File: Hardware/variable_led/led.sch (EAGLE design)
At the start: 12 parts

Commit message: Updated schematic labels and PCB layout based on feedback
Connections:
- net N$1 renamed 5V
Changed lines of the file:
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@@
 <setting verticaltext="up"/>
 </settings>
-<grid distance="0.1" unitdist="inch" unit="inch" style="lines" multiple="1" display="yes" altdistance="0.01" altunitdist="inch" altunit="inch"/>
+<grid distance="0.1" unitdist="inch" unit="inch" style="lines" multiple="1" display="no" altdistance="0.01" altunitdist="inch" altunit="inch"/>
 <layers>
 <layer number="1" name="Top" color="4" fill="1" visible="no" active="no"/>
@@
 </segment>
 </net>
-<net name="N$1" class="0">
+<net name="N$2" class="0">
+<segment>
+<wire x1="68.58" y1="50.8" x2="60.96" y2="50.8" width="0.1524" layer="91"/>
+<wire x1="60.96" y1="50.8" x2="60.96" y2="96.52" width="0.1524" layer="91"/>
+<wire x1="60.96" y1="96.52" x2="111.76" y2="96.52" width="0.1524" layer="91"/>
+<pinref part="R2" gate="G$1" pin="2"/>
+<wire x1="111.76" y1="96.52" x2="111.76" y2="78.74" width="0.1524" layer="91"/>
+<pinref part="JP1" gate="A" pin="13"/>
+</segment>
+</net>
+<net name="N$3" class="0">
+<segment>
+<pinref part="R2" gate="G$1" pin="1"/>
+<pinref part="LED1" gate="G$1" pin="A"/>
+<wire x1="111.76" y1="68.58" x2="111.76" y2="60.96" width="0.1524" layer="91"/>
+</segment>
+</net>
+<net name="N$4" class="0">
+<segment>
+<pinref part="SW1" gate="G$1" pin="P$1"/>
+<pinref part="R1" gate="G$1" pin="2"/>
+<wire x1="12.7" y1="22.86" x2="12.7" y2="20.32" width="0.1524" layer="91"/>
+<wire x1="12.7" y1="20.32" x2="58.42" y2="20.32" width="0.1524" layer="91"/>
+<wire x1="58.42" y1="20.32" x2="58.42" y2="81.28" width="0.1524" layer="91"/>
+<junction x="12.7" y="20.32"/>
+<pinref part="JP1" gate="A" pin="1"/>
+<wire x1="58.42" y1="81.28" x2="68.58" y2="81.28" width="0.1524" layer="91"/>
+</segment>
+</net>
+<net name="5V" class="0">
 <segment>
 <pinref part="IC1" gate="A" pin="OUT"/>
@@
 </segment>
 <segment>
+<pinref part="SW1" gate="G$1" pin="P$2"/>
+<wire x1="12.7" y1="33.02" x2="12.7" y2="38.1" width="0.1524" layer="91"/>
+<label x="12.7" y="38.1" size="1.778" layer="95" xref="yes"/>
+</segment>
+<segment>
 <pinref part="JP2" gate="A" pin="10"/>
 <wire x1="86.36" y1="58.42" x2="96.52" y2="58.42" width="0.1524" layer="91"/>
 <label x="96.52" y="58.42" size="1.778" layer="95" xref="yes"/>
 </segment>
-<segment>
-<pinref part="SW1" gate="G$1" pin="P$2"/>
-<wire x1="12.7" y1="33.02" x2="12.7" y2="38.1" width="0.1524" layer="91"/>
-<label x="12.7" y="38.1" size="1.778" layer="95" xref="yes"/>
-</segment>
-</net>
-<net name="N$2" class="0">
-<segment>
-<wire x1="68.58" y1="50.8" x2="60.96" y2="50.8" width="0.1524" layer="91"/>
-<wire x1="60.96" y1="50.8" x2="60.96" y2="96.52" width="0.1524" layer="91"/>
-<wire x1="60.96" y1="96.52" x2="111.76" y2="96.52" width="0.1524" layer="91"/>
-<pinref part="R2" gate="G$1" pin="2"/>
-<wire x1="111.76" y1="96.52" x2="111.76" y2="78.74" width="0.1524" layer="91"/>
-<pinref part="JP1" gate="A" pin="13"/>
-</segment>
-</net>
-<net name="N$3" class="0">
-<segment>
-<pinref part="R2" gate="G$1" pin="1"/>
-<pinref part="LED1" gate="G$1" pin="A"/>
-<wire x1="111.76" y1="68.58" x2="111.76" y2="60.96" width="0.1524" layer="91"/>
-</segment>
-</net>
-<net name="N$4" class="0">
-<segment>
-<pinref part="SW1" gate="G$1" pin="P$1"/>
-<pinref part="R1" gate="G$1" pin="2"/>
-<wire x1="12.7" y1="22.86" x2="12.7" y2="20.32" width="0.1524" layer="91"/>
-<wire x1="12.7" y1="20.32" x2="58.42" y2="20.32" width="0.1524" layer="91"/>
-<wire x1="58.42" y1="20.32" x2="58.42" y2="81.28" width="0.1524" layer="91"/>
-<junction x="12.7" y="20.32"/>
-<pinref part="JP1" gate="A" pin="1"/>
-<wire x1="58.42" y1="81.28" x2="68.58" y2="81.28" width="0.1524" layer="91"/>
-</segment>
-</net>
+</net>

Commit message: Updated PCB based on feedback
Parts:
- removed C1, C2: 10u, adafruit:C-USC0805
- removed C3, C4: 0.1u, adafruit:C-USC0805
- removed IC1: (no value), v-reg:78XXL
- added G1: AB9V, battery:AB9V
- added JP3: (no value), adafruit:PINHD-1X8BIG
- JP1: device adafruit:PINHD-1X18 -> adafruit:PINHD-1X8BIG
- JP2: device adafruit:PINHD-1X14 -> adafruit:PINHD-1X6B
- U$1: value 9V -> PINHD-1X10; device adafruit:CR1220SMT -> adafruit:PINHD-1X10
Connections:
- removed net V+: C1.1, C3.1, IC1.IN, U$1.+, U$1.+1
- net 5V: now also G1.+, JP3.4; no longer C2.1, C4.1, IC1.OUT, JP2.10
- net GND: now also G1.-, U$1.7; no longer C1.2, C2.2, C3.2, C4.2, IC1.GND, JP1.16, U$1.-
- net N$2: now also U$1.4; no longer JP1.13
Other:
- moved on the sheet: LED1, R1, R2, SW1

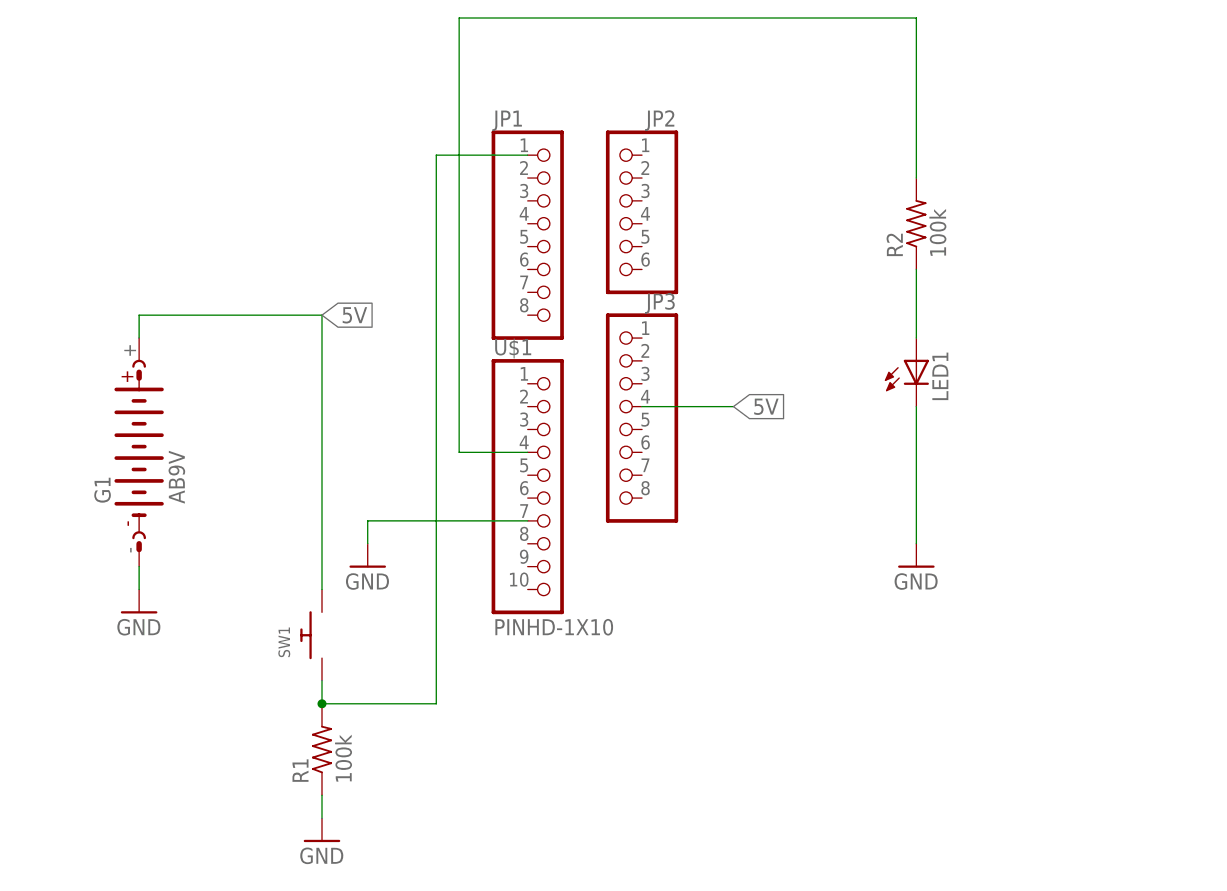
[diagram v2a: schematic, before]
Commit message: Changed LED to two pins and changed board to single side
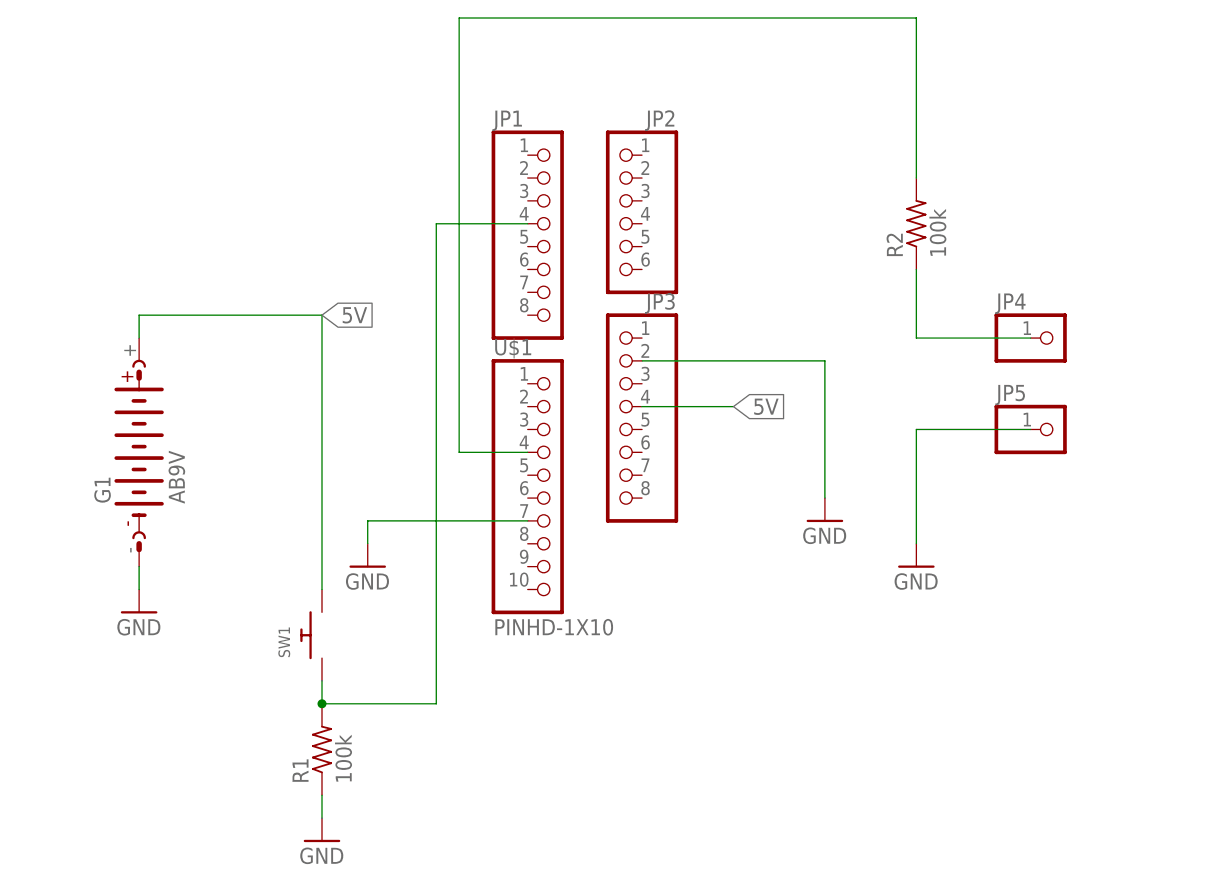
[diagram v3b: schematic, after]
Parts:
- removed LED1: (no value), adafruit:LED5MM
- added JP4, JP5: (no value), adafruit:PINHD-1X1
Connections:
- net GND: now also JP3.2, JP5.1; no longer LED1.C
- net N$3: now also JP4.1; no longer LED1.A
- net N$4: now also JP1.4; no longer JP1.1
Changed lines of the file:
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@@
 <part name="R1" library="adafruit" library_urn="urn:adsk.eagle:library:420" deviceset="R-US_" device="FLIPFLOP" package3d_urn="urn:adsk.eagle:package:6240726/1" value="100k"/>
 <part name="R2" library="adafruit" library_urn="urn:adsk.eagle:library:420" deviceset="R-US_" device="FLIPFLOP" package3d_urn="urn:adsk.eagle:package:6240726/1" value="100k"/>
-<part name="LED1" library="adafruit" library_urn="urn:adsk.eagle:library:420" deviceset="LED" device="5MM" package3d_urn="urn:adsk.eagle:package:6240538/1"/>
 <part name="GND1" library="supply1" library_urn="urn:adsk.eagle:library:371" deviceset="GND" device=""/>
 <part name="GND2" library="supply1" library_urn="urn:adsk.eagle:library:371" deviceset="GND" device=""/>
@@
 <part name="JP2" library="adafruit" library_urn="urn:adsk.eagle:library:420" deviceset="PINHD-1X6" device="B" package3d_urn="urn:adsk.eagle:package:6240714/1"/>
 <part name="JP3" library="adafruit" library_urn="urn:adsk.eagle:library:420" deviceset="PINHD-1X8" device="BIG" package3d_urn="urn:adsk.eagle:package:6240707/1"/>
+<part name="GND4" library="supply1" library_urn="urn:adsk.eagle:library:371" deviceset="GND" device=""/>
+<part name="JP4" library="adafruit" library_urn="urn:adsk.eagle:library:420" deviceset="PINHD-1X1" device="" package3d_urn="urn:adsk.eagle:package:6240654/1"/>
+<part name="JP5" library="adafruit" library_urn="urn:adsk.eagle:library:420" deviceset="PINHD-1X1" device="" package3d_urn="urn:adsk.eagle:package:6240654/1"/>
 </parts>
 <sheets>
@@
 <attribute name="NAME" x="82.3214" y="69.85" size="1.778" layer="95" rot="R90"/>
 <attribute name="VALUE" x="87.122" y="69.85" size="1.778" layer="96" rot="R90"/>
-</instance>
-<instance part="LED1" gate="G$1" x="83.82" y="58.42">
-<attribute name="NAME" x="87.376" y="53.848" size="1.778" layer="95" rot="R90"/>
-<attribute name="VALUE" x="89.535" y="53.848" size="1.778" layer="96" rot="R90"/>
 </instance>
 <instance part="GND1" gate="1" x="-2.54" y="30.48">
@@
 <attribute name="VALUE" x="57.15" y="38.1" size="1.778" layer="96" rot="MR0"/>
 </instance>
+<instance part="GND4" gate="1" x="73.66" y="40.64">
+<attribute name="VALUE" x="71.12" y="38.1" size="1.778" layer="96"/>
+</instance>
+<instance part="JP4" gate="G$1" x="99.06" y="60.96">
+<attribute name="NAME" x="92.71" y="64.135" size="1.778" layer="95"/>
+<attribute name="VALUE" x="92.71" y="55.88" size="1.778" layer="96"/>
+</instance>
+<instance part="JP5" gate="G$1" x="99.06" y="50.8">
+<attribute name="NAME" x="92.71" y="53.975" size="1.778" layer="95"/>
+<attribute name="VALUE" x="92.71" y="45.72" size="1.778" layer="96"/>
+</instance>
 </instances>
 <busses>
@@
 </segment>
 <segment>
-<pinref part="LED1" gate="G$1" pin="C"/>
 <pinref part="GND3" gate="1" pin="GND"/>
-<wire x1="83.82" y1="53.34" x2="83.82" y2="38.1" width="0.1524" layer="91"/>
+<pinref part="JP5" gate="G$1" pin="1"/>
+<wire x1="83.82" y1="50.8" x2="83.82" y2="38.1" width="0.1524" layer="91"/>
+<wire x1="96.52" y1="50.8" x2="83.82" y2="50.8" width="0.1524" layer="91"/>
 </segment>
 <segment>
@@
 <pinref part="GND2" gate="1" pin="GND"/>
 <wire x1="22.86" y1="40.64" x2="22.86" y2="38.1" width="0.1524" layer="91"/>
+</segment>
+<segment>
+<pinref part="JP3" gate="G$1" pin="2"/>
+<wire x1="53.34" y1="58.42" x2="73.66" y2="58.42" width="0.1524" layer="91"/>
+<wire x1="73.66" y1="58.42" x2="73.66" y2="43.18" width="0.1524" layer="91"/>
+<pinref part="GND4" gate="1" pin="GND"/>
 </segment>
 </net>
@@
 <segment>
 <pinref part="R2" gate="G$1" pin="1"/>
-<pinref part="LED1" gate="G$1" pin="A"/>
 <wire x1="83.82" y1="68.58" x2="83.82" y2="60.96" width="0.1524" layer="91"/>
+<pinref part="JP4" gate="G$1" pin="1"/>
+<wire x1="83.82" y1="60.96" x2="96.52" y2="60.96" width="0.1524" layer="91"/>
 </segment>
 </net>
@@
 <wire x1="17.78" y1="22.86" x2="17.78" y2="20.32" width="0.1524" layer="91"/>
 <wire x1="17.78" y1="20.32" x2="30.48" y2="20.32" width="0.1524" layer="91"/>
-<wire x1="30.48" y1="20.32" x2="30.48" y2="81.28" width="0.1524" layer="91"/>
+<wire x1="30.48" y1="20.32" x2="30.48" y2="73.66" width="0.1524" layer="91"/>
 <junction x="17.78" y="20.32"/>
-<wire x1="30.48" y1="81.28" x2="40.64" y2="81.28" width="0.1524" layer="91"/>
-<pinref part="JP1" gate="G$1" pin="1"/>
+<pinref part="JP1" gate="G$1" pin="4"/>
+<wire x1="40.64" y1="73.66" x2="30.48" y2="73.66" width="0.1524" layer="91"/>
 </segment>
 </net>
